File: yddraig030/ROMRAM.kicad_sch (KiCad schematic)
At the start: 14 parts

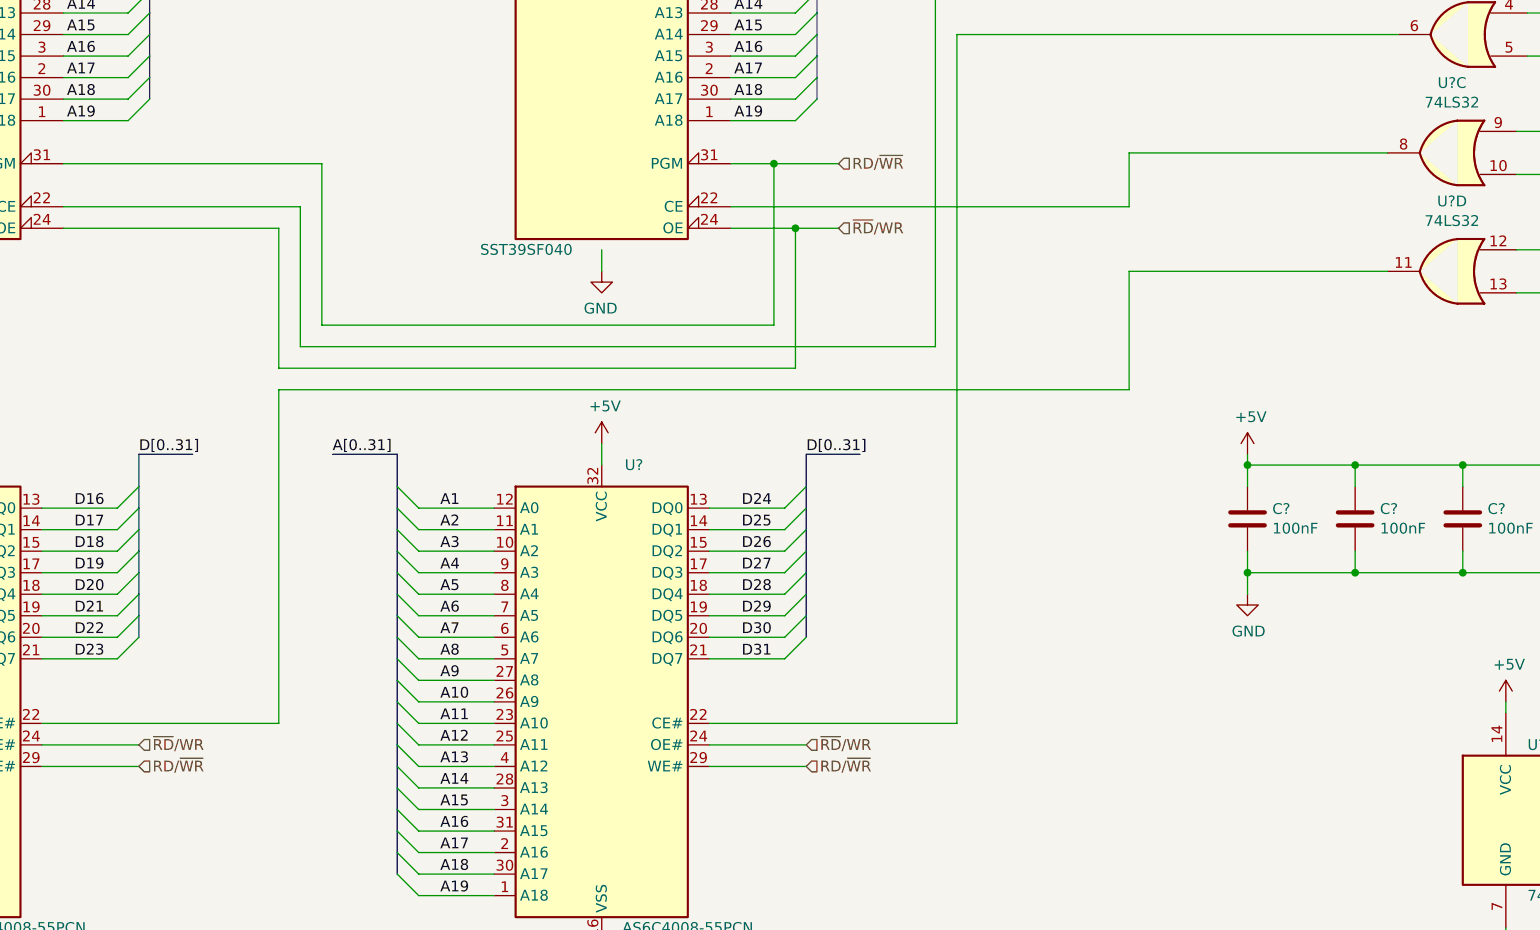
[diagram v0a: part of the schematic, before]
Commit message: More changes to the 030 board
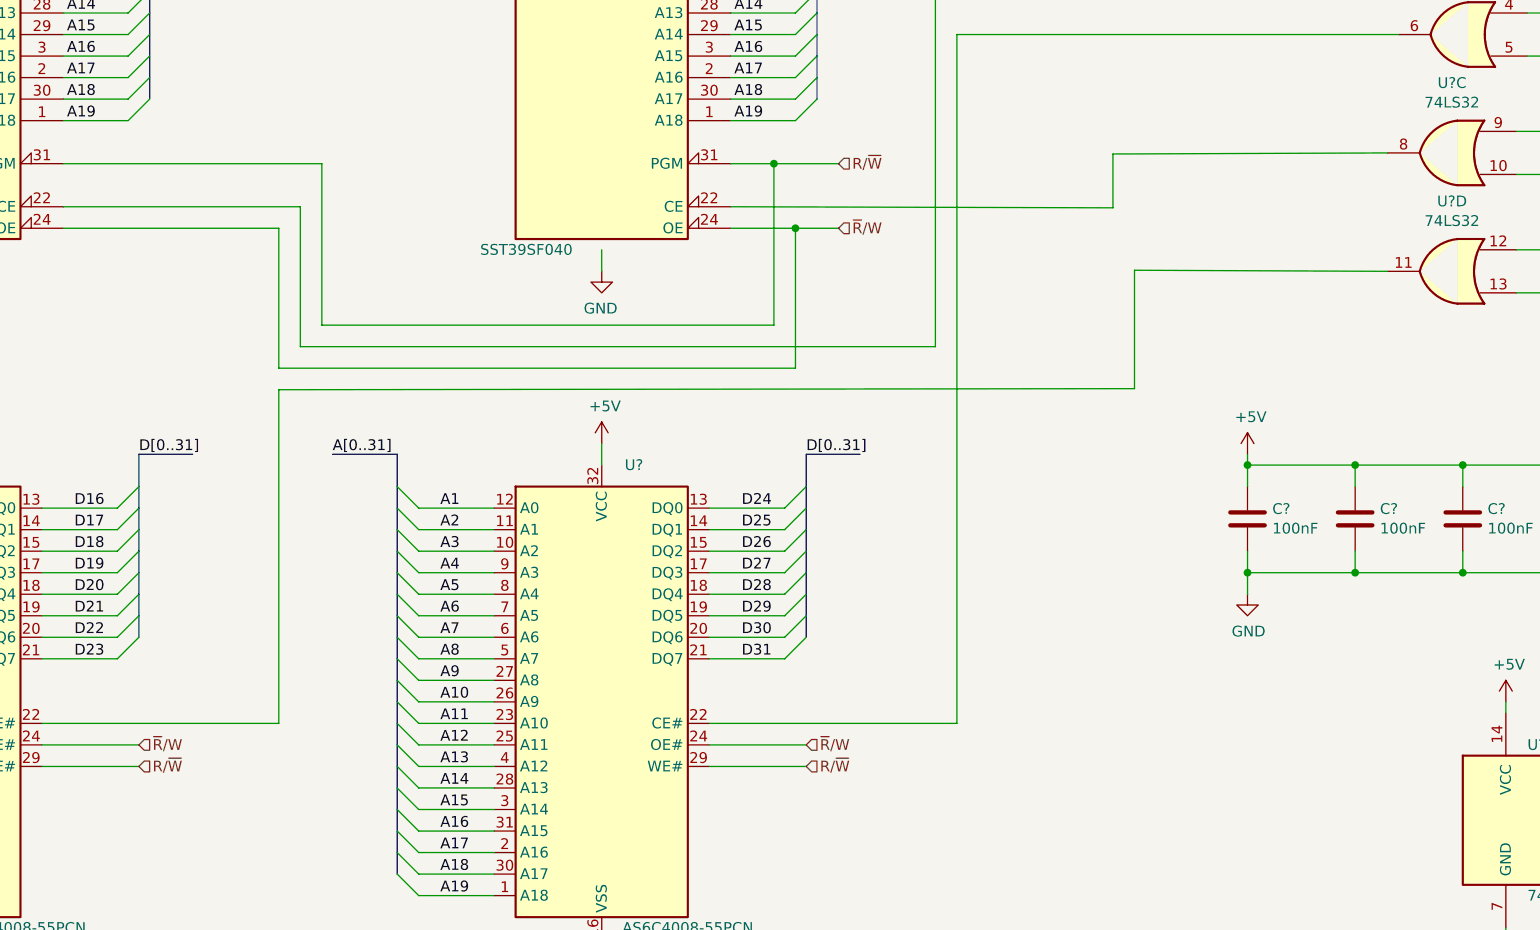
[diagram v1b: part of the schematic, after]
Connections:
- net RD/~{WR} renamed R/~{W}
- net ~{RD}/WR renamed ~{R}/W
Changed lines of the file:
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@@
     (stroke (width 0) (type default) (color 0 0 0 0))
   )
-  (wire (pts (xy 202.565 90.805) (xy 202.565 104.775))
+  (wire (pts (xy 203.2 90.678) (xy 203.2 104.648))
     (stroke (width 0) (type default) (color 0 0 0 0))
   )
@@
     (stroke (width 0) (type default) (color 0 0 0 0))
   )
-  (wire (pts (xy 233.045 90.805) (xy 202.565 90.805))
+  (wire (pts (xy 233.045 90.805) (xy 203.2 90.678))
     (stroke (width 0) (type default) (color 0 0 0 0))
   )
@@
     (stroke (width 0) (type default) (color 0 0 0 0))
   )
-  (wire (pts (xy 202.565 76.835) (xy 202.565 83.185))
+  (wire (pts (xy 200.66 76.962) (xy 200.66 83.312))
     (stroke (width 0) (type default) (color 0 0 0 0))
   )
@@
     (stroke (width 0) (type default) (color 0 0 0 0))
   )
-  (wire (pts (xy 155.575 83.185) (xy 202.565 83.185))
+  (wire (pts (xy 155.575 83.185) (xy 200.66 83.312))
     (stroke (width 0) (type default) (color 0 0 0 0))
   )
@@
     (stroke (width 0) (type default) (color 0 0 0 0))
   )
-  (wire (pts (xy 233.045 76.835) (xy 202.565 76.835))
+  (wire (pts (xy 233.045 76.835) (xy 200.66 76.962))
     (stroke (width 0) (type default) (color 0 0 0 0))
   )
@@
     (stroke (width 0) (type default) (color 0 0 0 0))
   )
-  (wire (pts (xy 102.235 104.775) (xy 202.565 104.775))
+  (wire (pts (xy 102.235 104.775) (xy 203.2 104.648))
     (stroke (width 0) (type default) (color 0 0 0 0))
   )
@@
     (effects (font (size 1.27 1.27)) (justify left bottom))
   )
-  (hierarchical_label "~{RD}{slash}WR" (shape input) (at 85.725 146.685 0)
+  (hierarchical_label "~{R}{slash}W" (shape input) (at 85.725 146.685 0)
     (effects (font (size 1.27 1.27)) (justify left))
   )
-  (hierarchical_label "~{RD}{slash}WR" (shape input) (at 164.465 146.685 0)
+  (hierarchical_label "~{R}{slash}W" (shape input) (at 164.465 146.685 0)
     (effects (font (size 1.27 1.27)) (justify left))
   )
@@
     (effects (font (size 1.27 1.27)) (justify left))
   )
-  (hierarchical_label "~{RD}{slash}WR" (shape input) (at 168.275 85.725 0)
+  (hierarchical_label "~{R}{slash}W" (shape input) (at 168.275 85.725 0)
     (effects (font (size 1.27 1.27)) (justify left))
   )
-  (hierarchical_label "RD{slash}~{WR}" (shape input) (at 85.725 149.225 0)
+  (hierarchical_label "R{slash}~{W}" (shape input) (at 85.725 149.225 0)
     (effects (font (size 1.27 1.27)) (justify left))
   )
@@
     (effects (font (size 1.27 1.27)) (justify left))
   )
-  (hierarchical_label "RD{slash}~{WR}" (shape input) (at 168.275 78.105 0)
+  (hierarchical_label "R{slash}~{W}" (shape input) (at 168.275 78.105 0)
     (effects (font (size 1.27 1.27)) (justify left))
   )
-  (hierarchical_label "RD{slash}~{WR}" (shape input) (at 164.465 149.225 0)
+  (hierarchical_label "R{slash}~{W}" (shape input) (at 164.465 149.225 0)
     (effects (font (size 1.27 1.27)) (justify left))
   )

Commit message: ddraig030 schematic done
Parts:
- gave numbers to parts that had none: 10
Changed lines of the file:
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@@
   (symbol (lib_id "power:GND") (at 247.015 169.545 0) (unit 1)
     (in_bom yes) (on_board yes)
-    (property "Reference" "#PWR?" (id 0) (at 247.015 175.895 0)
+    (property "Reference" "#PWR0412" (id 0) (at 247.015 175.895 0)
       (effects (font (size 1.27 1.27)) hide)
     )
@@
   (symbol (lib_id "power:GND") (at 61.595 170.815 0) (unit 1)
     (in_bom yes) (on_board yes)
-    (property "Reference" "#PWR?" (id 0) (at 61.595 177.165 0)
+    (property "Reference" "#PWR0404" (id 0) (at 61.595 177.165 0)
       (effects (font (size 1.27 1.27)) hide)
     )
@@
   (symbol (lib_id "power:+5V") (at 140.335 111.125 0) (unit 1)
     (in_bom yes) (on_board yes)
-    (property "Reference" "#PWR?" (id 0) (at 140.335 114.935 0)
+    (property "Reference" "#PWR0407" (id 0) (at 140.335 114.935 0)
       (effects (font (size 1.27 1.27)) hide)
     )
@@
   (symbol (lib_id "power:+5V") (at 61.595 111.125 0) (unit 1)
     (in_bom yes) (on_board yes)
-    (property "Reference" "#PWR?" (id 0) (at 61.595 114.935 0)
+    (property "Reference" "#PWR0403" (id 0) (at 61.595 114.935 0)
       (effects (font (size 1.27 1.27)) hide)
     )
@@
   (symbol (lib_id "power:+5V") (at 140.335 22.225 0) (mirror y) (unit 1)
     (in_bom yes) (on_board yes)
-    (property "Reference" "#PWR?" (id 0) (at 140.335 26.035 0)
+    (property "Reference" "#PWR0405" (id 0) (at 140.335 26.035 0)
       (effects (font (size 1.27 1.27)) hide)
     )
@@
   (symbol (lib_id "74xx:74LS32") (at 240.665 90.805 0) (mirror y) (unit 4)
     (in_bom yes) (on_board yes)
-    (property "Reference" "U?" (id 0) (at 240.665 82.55 0))
+    (property "Reference" "U405" (id 0) (at 240.665 82.55 0))
     (property "Value" "74LS32" (id 1) (at 240.665 84.8614 0))
     (property "Footprint" "Package_DIP:DIP-14_W7.62mm_Socket" (id 2) (at 240.665 90.805 0)
@@
   (symbol (lib_id "Memory_Flash:SST39SF040") (at 61.595 57.785 0) (mirror y) (unit 1)
     (in_bom yes) (on_board yes)
-    (property "Reference" "U?" (id 0) (at 56.515 24.765 0))
+    (property "Reference" "U401" (id 0) (at 56.515 24.765 0))
     (property "Value" "SST39SF040" (id 1) (at 52.705 88.265 0))
     (property "Footprint" "Package_DIP:DIP-32_W15.24mm_Socket" (id 2) (at 61.595 50.165 0)
@@
   (symbol (lib_id "Device:C") (at 254.635 120.015 0) (unit 1)
     (in_bom yes) (on_board yes)
-    (property "Reference" "C?" (id 0) (at 257.556 118.8466 0)
+    (property "Reference" "C404" (id 0) (at 257.556 118.8466 0)
       (effects (font (size 1.27 1.27)) (justify left))
     )
@@
   (symbol (lib_id "74xx:74LS32") (at 241.935 62.865 0) (mirror y) (unit 2)
     (in_bom yes) (on_board yes)
-    (property "Reference" "U?" (id 0) (at 241.935 54.61 0))
+    (property "Reference" "U405" (id 0) (at 241.935 54.61 0))
     (property "Value" "74LS32" (id 1) (at 241.935 56.9214 0))
     (property "Footprint" "Package_DIP:DIP-14_W7.62mm_Socket" (id 2) (at 241.935 62.865 0)
@@
   (symbol (lib_id "Device:C") (at 229.235 120.015 0) (unit 1)
     (in_bom yes) (on_board yes)
-    (property "Reference" "C?" (id 0) (at 232.156 118.8466 0)
+    (property "Reference" "C402" (id 0) (at 232.156 118.8466 0)
       (effects (font (size 1.27 1.27)) (justify left))
     )
@@
   (symbol (lib_id "Memory_RAM:AS6C4008-55PCN") (at 61.595 141.605 0) (unit 1)
     (in_bom yes) (on_board yes)
-    (property "Reference" "U?" (id 0) (at 65.405 113.665 0))
+    (property "Reference" "U402" (id 0) (at 65.405 113.665 0))
     (property "Value" "AS6C4008-55PCN" (id 1) (at 71.755 168.275 0))
     (property "Footprint" "Package_DIP:DIP-32_W15.24mm_Socket" (id 2) (at 61.595 139.065 0)
@@
   (symbol (lib_id "74xx:74LS32") (at 241.935 48.895 0) (mirror y) (unit 1)
     (in_bom yes) (on_board yes)
-    (property "Reference" "U?" (id 0) (at 241.935 40.64 0))
+    (property "Reference" "U405" (id 0) (at 241.935 40.64 0))
     (property "Value" "74LS32" (id 1) (at 241.935 42.9514 0))
     (property "Footprint" "Package_DIP:DIP-14_W7.62mm_Socket" (id 2) (at 241.935 48.895 0)
@@
   (symbol (lib_id "Memory_Flash:SST39SF040") (at 140.335 57.785 0) (mirror y) (unit 1)
     (in_bom yes) (on_board yes)
-    (property "Reference" "U?" (id 0) (at 135.255 24.765 0))
+    (property "Reference" "U403" (id 0) (at 135.255 24.765 0))
     (property "Value" "SST39SF040" (id 1) (at 131.445 88.265 0))
     (property "Footprint" "Package_DIP:DIP-32_W15.24mm_Socket" (id 2) (at 140.335 50.165 0)
@@
   (symbol (lib_id "power:GND") (at 140.335 170.815 0) (unit 1)
     (in_bom yes) (on_board yes)
-    (property "Reference" "#PWR?" (id 0) (at 140.335 177.165 0)
+    (property "Reference" "#PWR0408" (id 0) (at 140.335 177.165 0)
       (effects (font (size 1.27 1.27)) hide)
     )
@@
   (symbol (lib_id "Device:C") (at 216.535 120.015 0) (unit 1)
     (in_bom yes) (on_board yes)
-    (property "Reference" "C?" (id 0) (at 219.456 118.8466 0)
+    (property "Reference" "C401" (id 0) (at 219.456 118.8466 0)
       (effects (font (size 1.27 1.27)) (justify left))
     )
@@
   (symbol (lib_id "power:+5V") (at 61.595 22.225 0) (mirror y) (unit 1)
     (in_bom yes) (on_board yes)
-    (property "Reference" "#PWR?" (id 0) (at 61.595 26.035 0)
+    (property "Reference" "#PWR0401" (id 0) (at 61.595 26.035 0)
       (effects (font (size 1.27 1.27)) hide)
     )
@@
   (symbol (lib_id "power:+5V") (at 216.535 112.395 0) (unit 1)
     (in_bom yes) (on_board yes)
-    (property "Reference" "#PWR?" (id 0) (at 216.535 116.205 0)
+    (property "Reference" "#PWR0409" (id 0) (at 216.535 116.205 0)
       (effects (font (size 1.27 1.27)) hide)
     )
@@
   (symbol (lib_id "Device:C") (at 241.935 120.015 0) (unit 1)
     (in_bom yes) (on_board yes)
-    (property "Reference" "C?" (id 0) (at 244.856 118.8466 0)
+    (property "Reference" "C403" (id 0) (at 244.856 118.8466 0)
       (effects (font (size 1.27 1.27)) (justify left))
     )
@@
   (symbol (lib_id "Device:C") (at 267.335 120.015 0) (unit 1)
     (in_bom yes) (on_board yes)
-    (property "Reference" "C?" (id 0) (at 270.256 118.8466 0)
+    (property "Reference" "C405" (id 0) (at 270.256 118.8466 0)
       (effects (font (size 1.27 1.27)) (justify left))
     )
@@
   (symbol (lib_id "power:GND") (at 216.535 128.905 0) (unit 1)
     (in_bom yes) (on_board yes)
-    (property "Reference" "#PWR?" (id 0) (at 216.535 135.255 0)
+    (property "Reference" "#PWR0410" (id 0) (at 216.535 135.255 0)
       (effects (font (size 1.27 1.27)) hide)
     )
@@
   (symbol (lib_id "Memory_RAM:AS6C4008-55PCN") (at 140.335 141.605 0) (unit 1)
     (in_bom yes) (on_board yes)
-    (property "Reference" "U?" (id 0) (at 144.145 113.665 0))
+    (property "Reference" "U404" (id 0) (at 144.145 113.665 0))
     (property "Value" "AS6C4008-55PCN" (id 1) (at 150.495 168.275 0))
     (property "Footprint" "Package_DIP:DIP-32_W15.24mm_Socket" (id 2) (at 140.335 139.065 0)
@@
   (symbol (lib_id "power:+5V") (at 247.015 141.605 0) (unit 1)
     (in_bom yes) (on_board yes)
-    (property "Reference" "#PWR?" (id 0) (at 247.015 145.415 0)
+    (property "Reference" "#PWR0411" (id 0) (at 247.015 145.415 0)
       (effects (font (size 1.27 1.27)) hide)
     )
@@
   (symbol (lib_id "74xx:74LS32") (at 240.665 76.835 0) (mirror y) (unit 3)
     (in_bom yes) (on_board yes)
-    (property "Reference" "U?" (id 0) (at 240.665 68.58 0))
+    (property "Reference" "U405" (id 0) (at 240.665 68.58 0))
     (property "Value" "74LS32" (id 1) (at 240.665 70.8914 0))
     (property "Footprint" "Package_DIP:DIP-14_W7.62mm_Socket" (id 2) (at 240.665 76.835 0)
@@
   (symbol (lib_id "74xx:74LS32") (at 247.015 155.575 0) (unit 5)
     (in_bom yes) (on_board yes)
-    (property "Reference" "U?" (id 0) (at 249.555 146.685 0)
+    (property "Reference" "U405" (id 0) (at 249.555 146.685 0)
       (effects (font (size 1.27 1.27)) (justify left))
     )
@@
   (symbol (lib_id "power:GND") (at 61.595 90.805 0) (mirror y) (unit 1)
     (in_bom yes) (on_board yes)
-    (property "Reference" "#PWR?" (id 0) (at 61.595 97.155 0)
+    (property "Reference" "#PWR0402" (id 0) (at 61.595 97.155 0)
       (effects (font (size 1.27 1.27)) hide)
     )
@@
   (symbol (lib_id "power:GND") (at 140.335 90.805 0) (mirror y) (unit 1)
     (in_bom yes) (on_board yes)
-    (property "Reference" "#PWR?" (id 0) (at 140.335 97.155 0)
-      (effects (font (size 1.27 1.27)) hide)
-    )
+    (property "Reference" "#PWR0406" (id 0) (at 140.335 97.155 0)
+      (effects (font (size 1.27 1.27)) hide)
+    )

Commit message: yddraig030: Fixed ERC check errors
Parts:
- U402, U404: footprint Package_DIP:DIP-32_W15.24mm_Socket -> Package_DIP:DIP-32_W15.24mm
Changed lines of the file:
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@@
     (effects (font (size 1.27 1.27)) (justify left))
   )
-  (hierarchical_label "A[0..31]" (shape input) (at 110.49 22.225 180)
+  (hierarchical_label "D[0..31]" (shape bidirectional) (at 110.49 22.225 180)
     (effects (font (size 1.27 1.27)) (justify right))
   )
@@
     (effects (font (size 1.27 1.27)) (justify left))
   )
-  (hierarchical_label "D[0..31]" (shape bidirectional) (at 168.275 22.225 0)
+  (hierarchical_label "A[0..31]" (shape input) (at 168.275 22.225 0)
     (effects (font (size 1.27 1.27)) (justify left))
   )
@@
     (property "Reference" "U402" (id 0) (at 65.405 113.665 0))
     (property "Value" "AS6C4008-55PCN" (id 1) (at 71.755 168.275 0))
-    (property "Footprint" "Package_DIP:DIP-32_W15.24mm_Socket" (id 2) (at 61.595 139.065 0)
+    (property "Footprint" "Package_DIP:DIP-32_W15.24mm" (id 2) (at 61.595 139.065 0)
       (effects (font (size 1.27 1.27)) hide)
     )
@@
     (property "Reference" "U404" (id 0) (at 144.145 113.665 0))
     (property "Value" "AS6C4008-55PCN" (id 1) (at 150.495 168.275 0))
-    (property "Footprint" "Package_DIP:DIP-32_W15.24mm_Socket" (id 2) (at 140.335 139.065 0)
-      (effects (font (size 1.27 1.27)) hide)
-    )
+    (property "Footprint" "Package_DIP:DIP-32_W15.24mm" (id 2) (at 140.335 139.065 0)
+      (effects (font (size 1.27 1.27)) hide)
+    )

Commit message: More changes in yddraig030 layout
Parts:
- removed C404, C405: 100nF, Capacitor_THT:C_Disc_D3.8mm_W2.6mm_P2.50mm, symbol Device:C
- removed U402, U404: AS6C4008-55PCN, Package_DIP:DIP-32_W15.24mm, symbol Memory_RAM:AS6C4008-55PCN
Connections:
- net ~{CS_SRAM} is gone; now on net GND: U405.13, U405.5
- net GND: now also U405.12, U405.4
- net ~{LDS}: now also U405.9; no longer U405.1, U405.4
- net ~{UDS}: now also U405.1; no longer U405.12, U405.9
- net at U401.22 (CE): now also U405.8; no longer U405.3
- net at U403.22 (CE): now also U405.3; no longer U405.8
- no-connect marks 0 -> 2
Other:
- moved on the sheet: C401, C402, C403, U401, U403, U405A, U405B, U405C, U405D, U405E
